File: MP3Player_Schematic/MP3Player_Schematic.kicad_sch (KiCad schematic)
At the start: 5 parts, among them J1 Rotary encoder

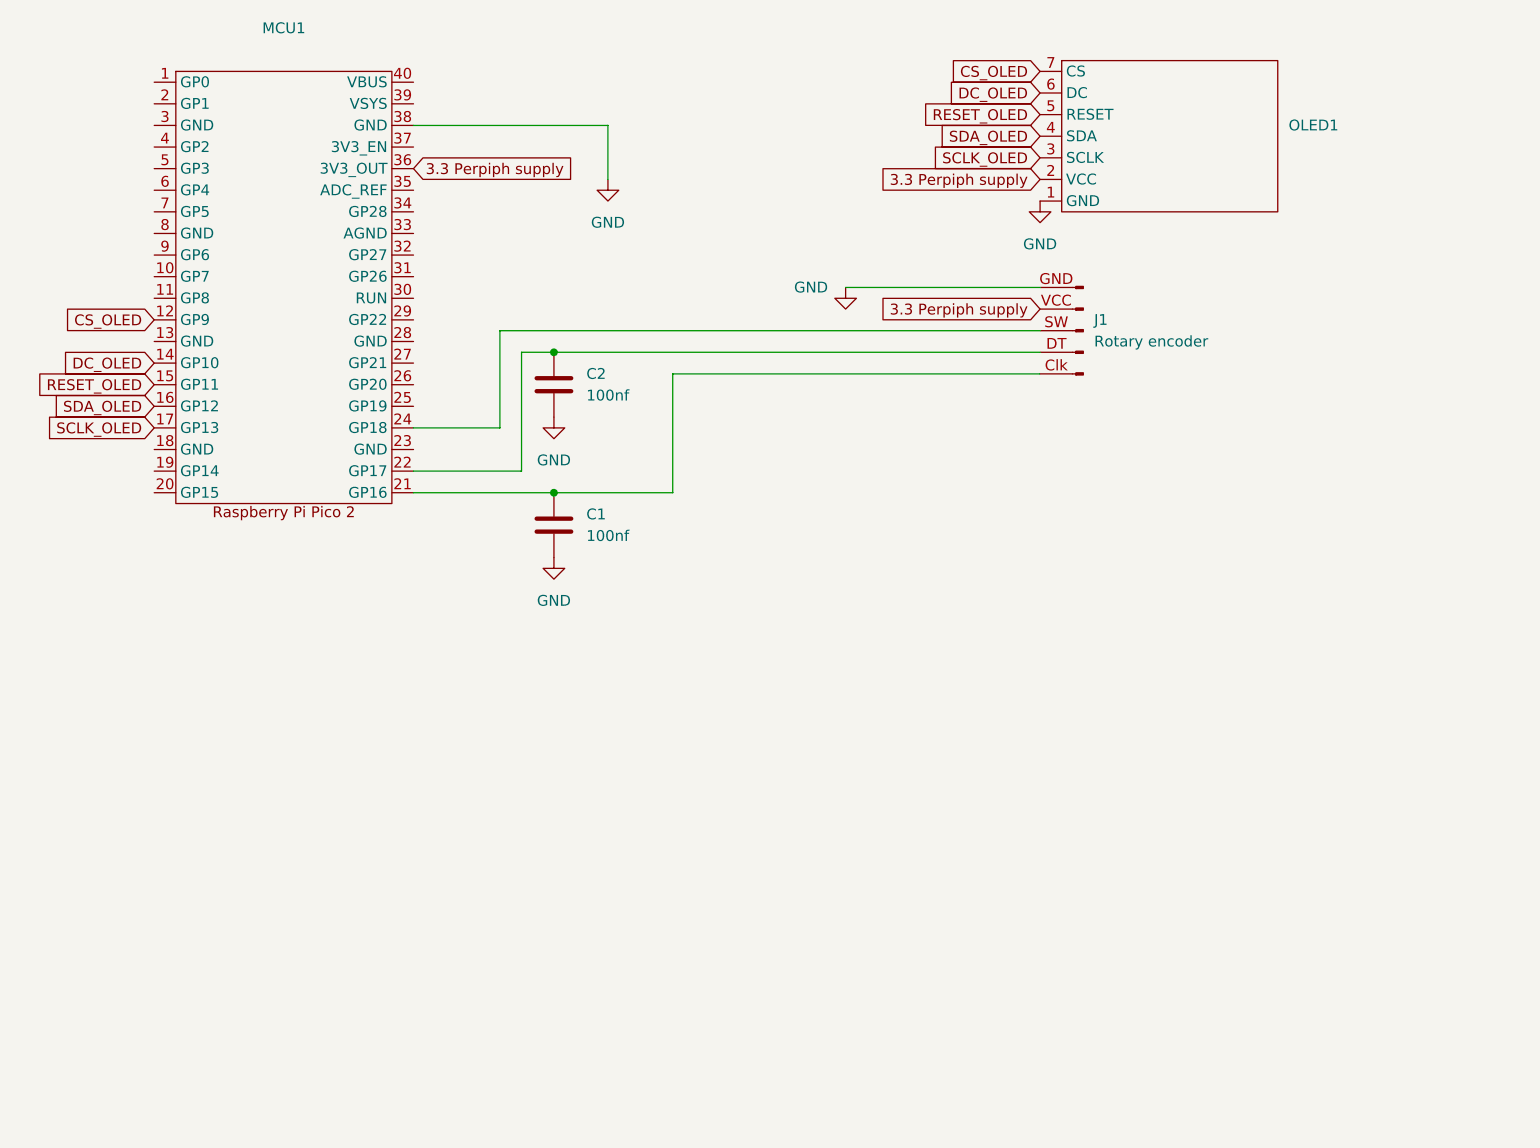
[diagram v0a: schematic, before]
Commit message: added OLED screen type with array holding all screens, encoder now switches active selection
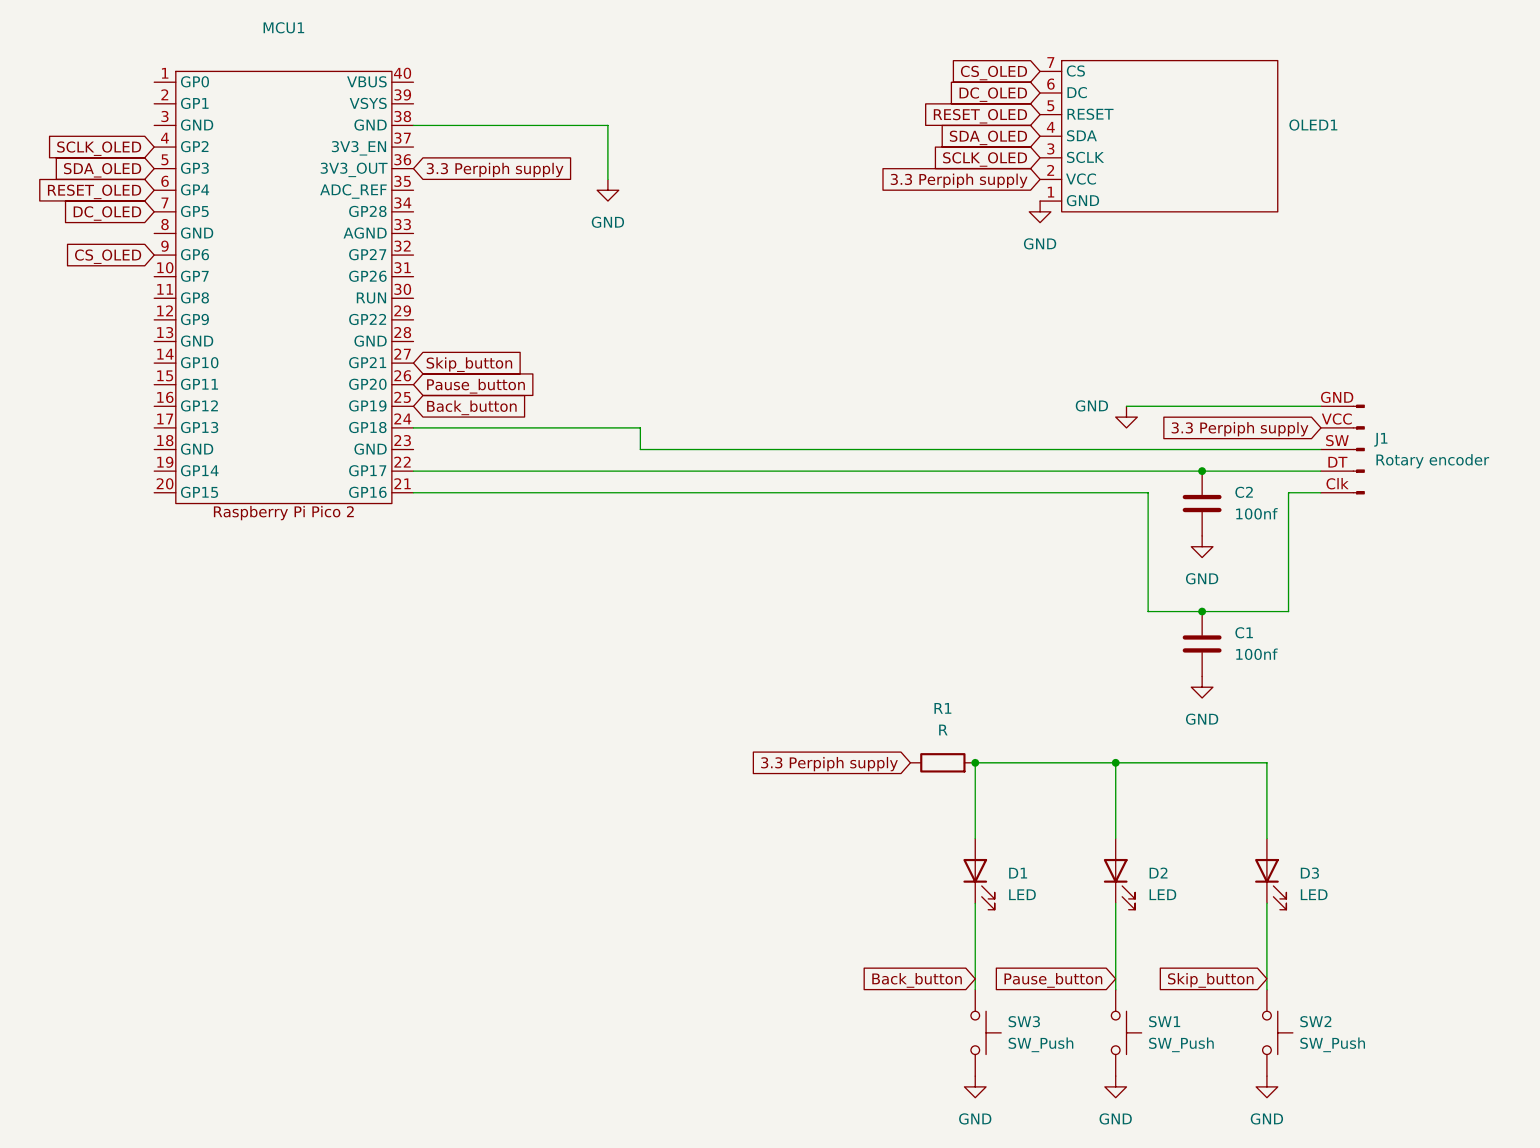
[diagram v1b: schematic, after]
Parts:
- added D1, D2, D3: LED, symbol Device:LED
- added R1: R, symbol Device:R
- added SW1, SW2, SW3: SW_Push, symbol Switch:SW_Push
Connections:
- net 3.3 Perpiph supply: now also R1.1
- net CS_OLED: now also MCU1.9 (GP6); no longer MCU1.12 (GP9)
- net DC_OLED: now also MCU1.7 (GP5); no longer MCU1.14 (GP10)
- net GND: now also SW1.2, SW2.2, SW3.2
- net RESET_OLED: now also MCU1.6 (GP4); no longer MCU1.15 (GP11)
- net SCLK_OLED: now also MCU1.4 (GP2); no longer MCU1.17 (GP13)
- net SDA_OLED: now also MCU1.5 (GP3); no longer MCU1.16 (GP12)
- net Back_button: now reaches MCU1.25 (GP19)
- net Back_button: now also D1.1 (K), SW3.1
- net Pause_button: now reaches MCU1.26 (GP20)
- net Pause_button: now also D2.1 (K), SW1.1
- net Skip_button: now reaches MCU1.27 (GP21)
- net Skip_button: now also D3.1 (K), SW2.1
- new net: D1.2 (A), D2.2 (A), D3.2 (A), R1.2
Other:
- moved on the sheet: C1, C2, J1

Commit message: improved state mechine
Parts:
- added U1: VS1053B, VS1053B:LQFP48, symbol Imports:VS1053B
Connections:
- net at MCU1.23 (GND): now also J1.SW (Pin_3)
- net at MCU1.24 (GP18): no longer J1.SW (Pin_3)
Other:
- moved on the sheet: C1, C2, D1, D2, D3, J1, MCU1, OLED1, R1, SW1, SW2, SW3

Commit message: idk
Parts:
- removed J1: Rotary encoder, symbol Connector:Conn_01x05_Pin
- removed MCU1: ~, symbol Imports:RasPiPico2
- removed U1: VS1053B, VS1053B:LQFP48, symbol Imports:VS1053B
- added C3: 100nF, symbol Device:C
- added C4, C5: 10pF, symbol Device:C
- added R2, R3, R4: 10K, symbol Device:R
- added R5: 1M, symbol Device:R
- added SW4: RotaryEncoder_Switch, symbol Device:RotaryEncoder_Switch
- added U1: RP2350_60QFN, RP2350_60QFN_minimal:RP2350-QFN-60-1EP_7x7_P0.4mm_EP3.4x3.4mm_ThermalVias, symbol Imports:RP2350_60QFN
- added U2: VS1053B, VS1053B:LQFP48, symbol Imports:VS1053B
- added Y1: Crystal, symbol Device:Crystal
- C1, C2: value 100nf -> 100nF
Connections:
- net Back_button: now also U1.31 (GPIO19)
- net CS_OLED: now also U1.12 (GPIO8)
- net DC_OLED: now also U1.10 (GPIO7)
- net GND: now also C1.1, C2.1, C3.1, C4.2, C5.2, SW4.C, SW4.S2, U1.61 (GND); no longer C1.2, C2.2
- net Pause_button: now also U1.32 (GPIO20)
- net RESET_OLED: now also U1.9 (GPIO6)
- net Skip_button: now also U1.33 (GPIO21)
- net 3.3 Perpiph supply renamed Vcc
- net Vcc: now also R2.2, R3.2, R4.2, U1.45 (IOVDD)
- net SCLK_OLED renamed SCLK
- net SCLK: now also U1.4 (GPIO2), U2.28 (SCLK)
- net SDA_OLED renamed MOSI
- net MOSI: now also U1.5 (GPIO3), U2.29 (SI)
- new net: C5.1, R5.2, U2.17 (XTALO), Y1.1
- new net: C4.1, R5.1, U2.18 (XTALI/MCLK), Y1.2
- new net MISO: U1.7 (GPIO4), U2.30 (SO)
- new net Rotary_Clk: C1.2, R2.1, SW4.A, U1.27 (GPIO16)
- new net Rotary_DT: C2.2, R3.1, SW4.B, U1.28 (GPIO17)
- new net Rotary_sw: C3.2, R4.1, SW4.S1, U1.29 (GPIO18)
